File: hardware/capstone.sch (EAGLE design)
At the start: 30 parts, among them J1 61300311121, J2 61300311121, U1 BMP388, U2 LSM9DS1TR, U3 RFM95W-915S2

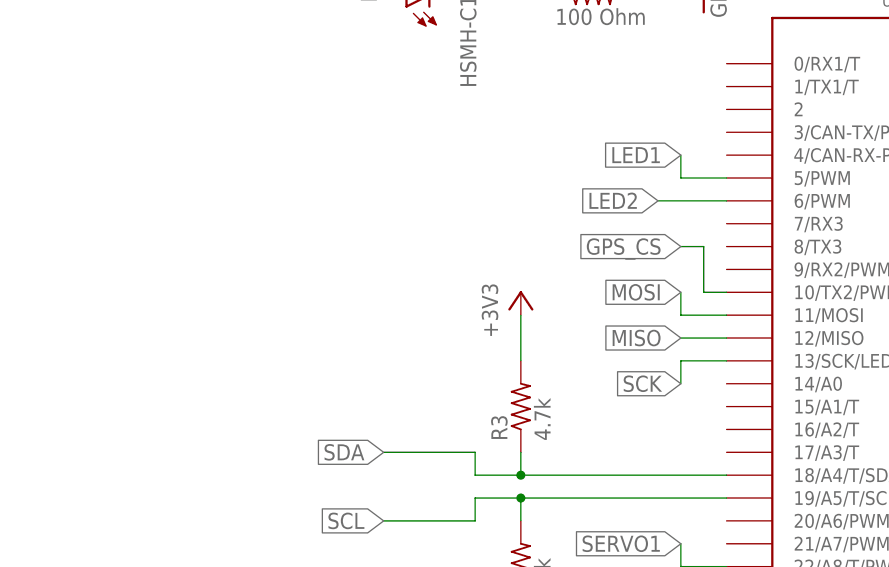
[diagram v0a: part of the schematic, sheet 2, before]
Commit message: Finished board routing
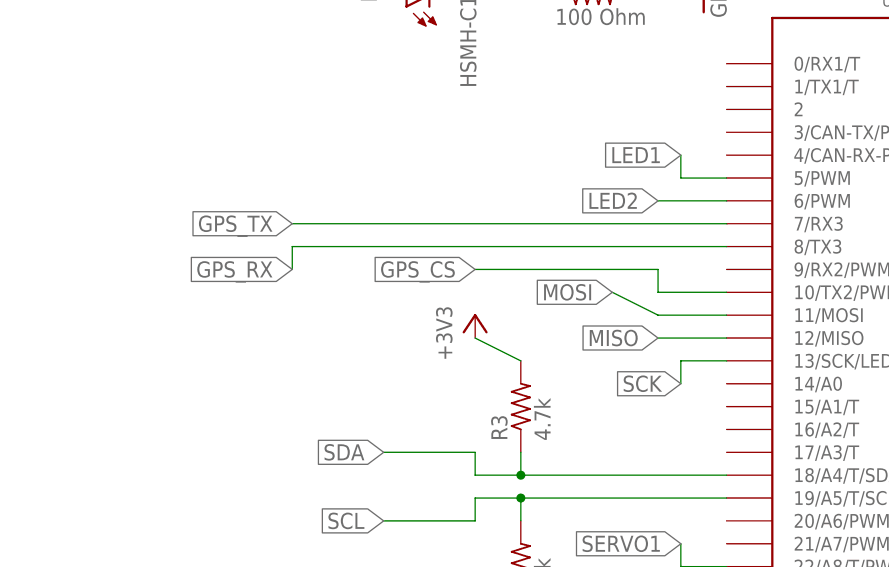
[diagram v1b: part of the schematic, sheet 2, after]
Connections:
- net GPS_RX: now also U$1.8/TX3
- net GPS_TX: now also U$1.7/RX3

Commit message: Finalize board
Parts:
- renumbered D1 to PWR_LED, D4 to FIX_LED
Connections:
- removed net ANT1: ANT1.1, U3.ANT
- net GND: now also ANT1.1, U3.ANT
